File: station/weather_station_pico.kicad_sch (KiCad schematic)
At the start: 12 parts, among them J1 I2C1_EXP, J2 I2C0_EXP, U1 Pico

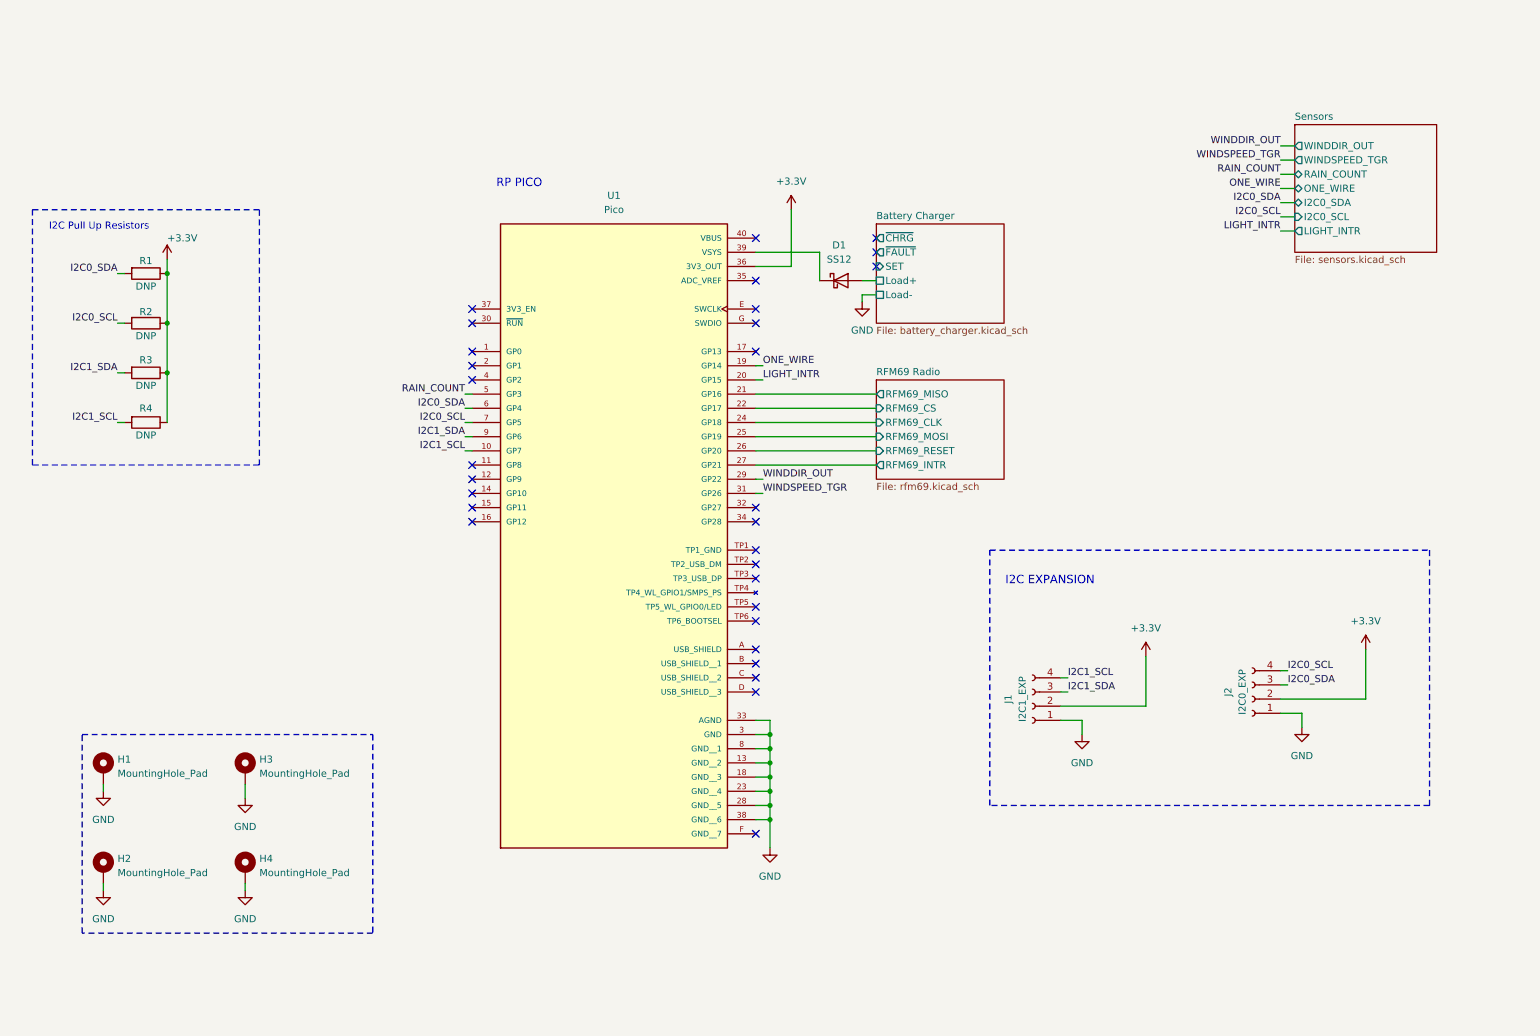
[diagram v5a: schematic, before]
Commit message: Added a reset button, status LEDs and broke out UART pins
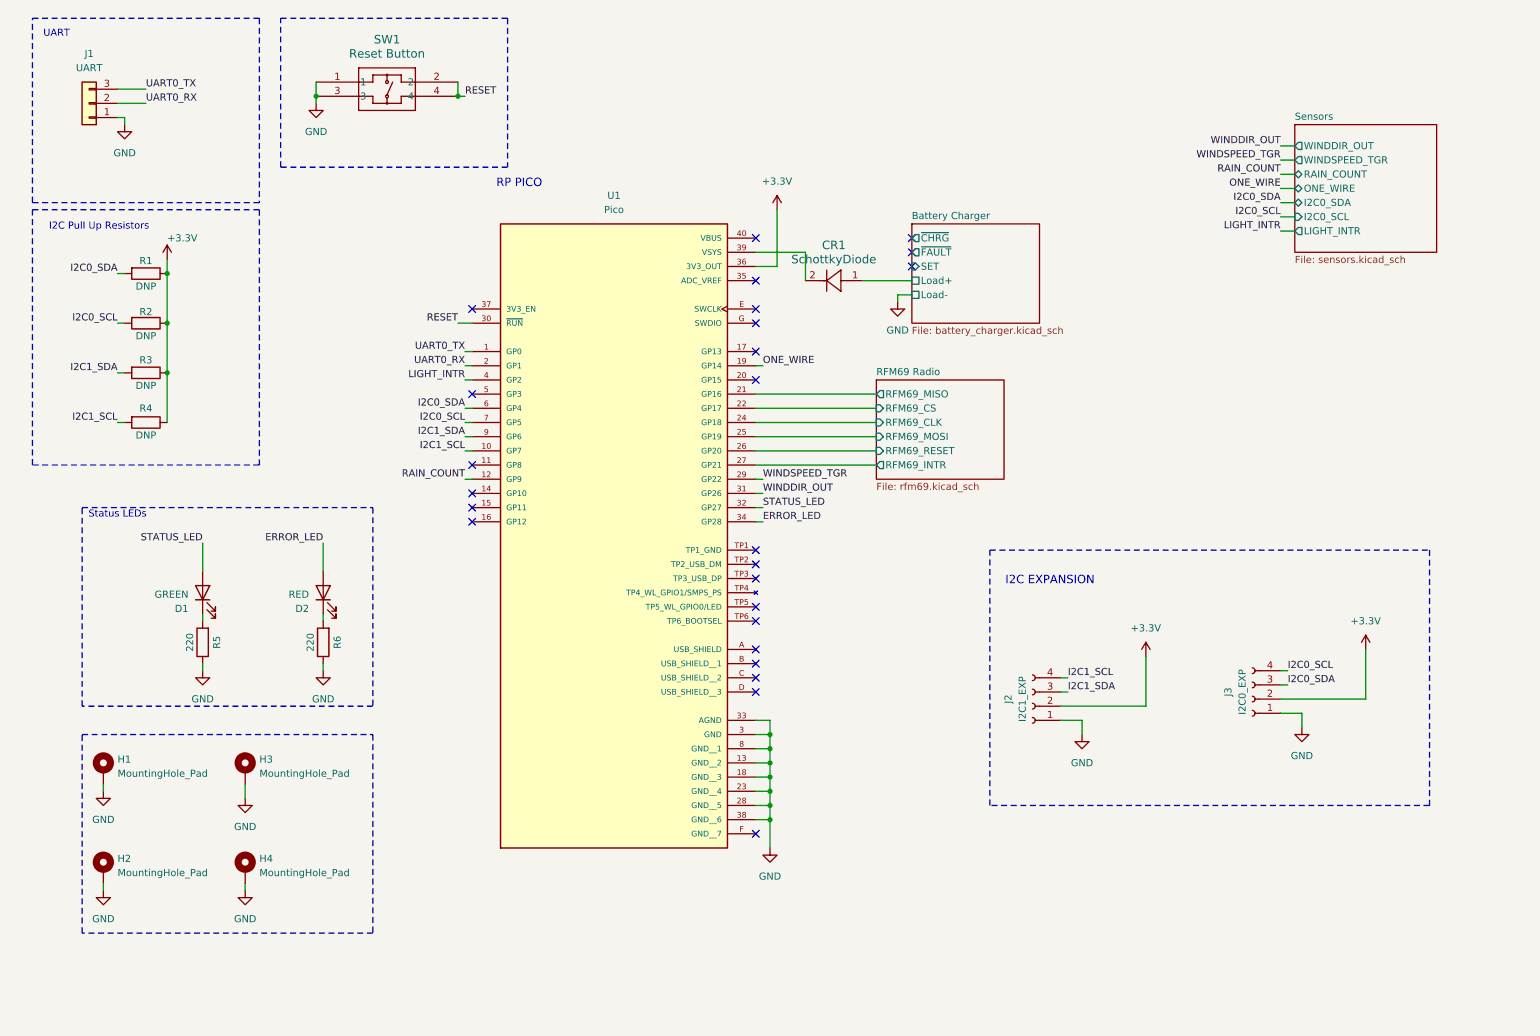
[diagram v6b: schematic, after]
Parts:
- removed D1: SS12, Diode_SMD:D_SMA, symbol Diode:SS12
- added CR1: SchottkyDiode, WeatherStation:SchottkyDiode, symbol Weather_Sensors:SchottkyDiode
- added D1: GREEN, LED_SMD:LED_0805_2012Metric_Pad1.15x1.40mm_HandSolder, symbol Device:LED
- added D2: RED, LED_SMD:LED_0805_2012Metric_Pad1.15x1.40mm_HandSolder, symbol Device:LED
- added J1: UART, Connector_PinSocket_2.54mm:PinSocket_1x03_P2.54mm_Vertical, symbol Connector_Generic:Conn_01x03
- added R5, R6: 220, Resistor_SMD:R_0805_2012Metric_Pad1.20x1.40mm_HandSolder, symbol Device:R
- added SW1: Reset Button, WeatherStation:TactileButton, symbol Weather_Sensors:TactileButton
- renumbered J1 to J2, J2 to J3
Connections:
- net Battery Charger/Load+: now also CR1.1
- net GND: now also J1.1 (Pin_1), R5.1, R6.1, SW1.1, SW1.3
- net LIGHT_INTR: now also U1.4 (GP2); no longer U1.20 (GP15)
- net RAIN_COUNT: now also U1.12 (GP9); no longer U1.5 (GP3)
- net WINDDIR_OUT: now also U1.31 (GP26); no longer U1.29 (GP22)
- net WINDSPEED_TGR: now also U1.29 (GP22); no longer U1.31 (GP26)
- net at U1.39 (VSYS): now also CR1.2
- net UART0_TX: now reaches U1.1 (GP0)
- net UART0_TX: now also J1.3 (Pin_3)
- net UART0_RX: now reaches U1.2 (GP1)
- net UART0_RX: now also J1.2 (Pin_2)
- net RESET: now reaches U1.30 (~{RUN})
- net RESET: now also SW1.2, SW1.4
- net STATUS_LED: now reaches U1.32 (GP27)
- net STATUS_LED: now also D1.2 (A)
- net ERROR_LED: now reaches U1.34 (GP28)
- net ERROR_LED: now also D2.2 (A)
- new net: D1.1 (K), R5.2
- new net: D2.1 (K), R6.2
- no-connect marks 30 -> 25
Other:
- note added: "Status LEDs"
- note added: "UART"

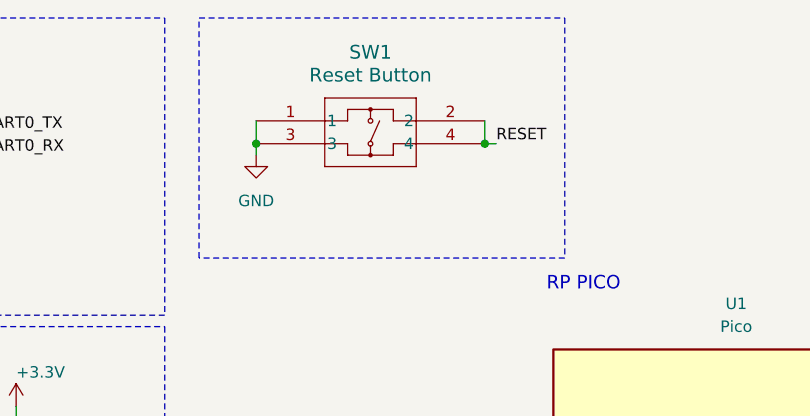
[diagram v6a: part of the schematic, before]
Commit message: Fixed a defect where to wrong pins of the reset button were shorted together, causing the pico board to be in a constant reset state
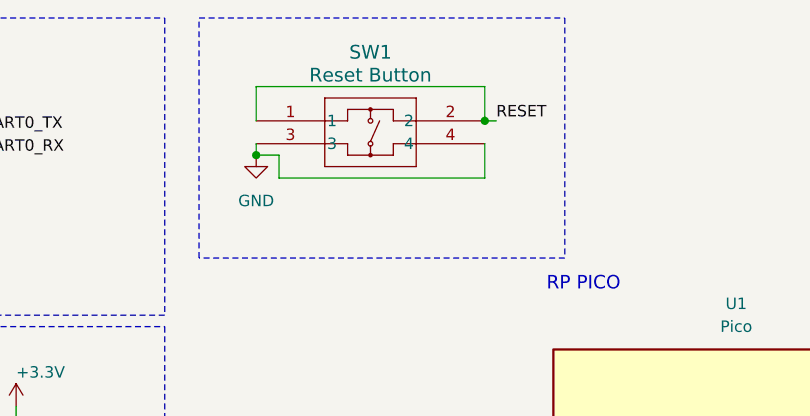
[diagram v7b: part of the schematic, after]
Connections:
- net GND: now also SW1.4; no longer SW1.1
- net RESET: now also SW1.1; no longer SW1.4
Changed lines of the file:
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@@
+	)
+	(junction
+		(at 67.31 29.21)
+		(diameter 0)
+		(color 0 0 0 0)
+	)
+	(junction
+		(at 92.71 25.4)
+		(diameter 0)
+		(color 0 0 0 0)
 	)
 	(junction
@@
 	)
 	(junction
-		(at 67.31 27.94)
-		(diameter 0)
-		(color 0 0 0 0)
-	)
-	(junction
 		(at 148.59 157.48)
-		(diameter 0)
-		(color 0 0 0 0)
-	)
-	(junction
-		(at 92.71 27.94)
 		(diameter 0)
 		(color 0 0 0 0)
@@
 	(wire
 		(pts
+			(xy 69.85 29.21) (xy 67.31 29.21)
+		)
+		(stroke
+			(width 0)
+			(type default)
+		)
+	)
+	(wire
+		(pts
 			(xy 68.58 113.03) (xy 68.58 107.95)
 		)
@@
 	(wire
 		(pts
-			(xy 92.71 25.4) (xy 92.71 27.94)
-		)
-		(stroke
-			(width 0)
-			(type default)
-		)
-	)
-	(wire
-		(pts
 			(xy 146.05 142.24) (xy 148.59 142.24)
 		)
@@
 	(wire
 		(pts
-			(xy 67.31 25.4) (xy 67.31 27.94)
-		)
-		(stroke
-			(width 0)
-			(type default)
-		)
-	)
-	(wire
-		(pts
 			(xy 93.98 88.9) (xy 95.25 88.9)
 		)
@@
 	(wire
 		(pts
-			(xy 92.71 27.94) (xy 93.98 27.94)
-		)
-		(stroke
-			(width 0)
-			(type default)
-		)
-	)
-	(wire
-		(pts
 			(xy 93.98 78.74) (xy 95.25 78.74)
 		)
@@
 	(wire
 		(pts
+			(xy 92.71 27.94) (xy 92.71 31.75)
+		)
+		(stroke
+			(width 0)
+			(type default)
+		)
+	)
+	(wire
+		(pts
 			(xy 31.75 86.36) (xy 33.02 86.36)
 		)
@@
 	(wire
 		(pts
+			(xy 67.31 21.59) (xy 92.71 21.59)
+		)
+		(stroke
+			(width 0)
+			(type default)
+		)
+	)
+	(wire
+		(pts
+			(xy 92.71 25.4) (xy 93.98 25.4)
+		)
+		(stroke
+			(width 0)
+			(type default)
+		)
+	)
+	(wire
+		(pts
 			(xy 240.03 135.89) (xy 255.27 135.89)
 		)
@@
 	(wire
 		(pts
+			(xy 67.31 25.4) (xy 67.31 21.59)
+		)
+		(stroke
+			(width 0)
+			(type default)
+		)
+	)
+	(wire
+		(pts
 			(xy 146.05 101.6) (xy 147.32 101.6)
 		)
@@
 	(wire
 		(pts
+			(xy 92.71 21.59) (xy 92.71 25.4)
+		)
+		(stroke
+			(width 0)
+			(type default)
+		)
+	)
+	(wire
+		(pts
+			(xy 69.85 31.75) (xy 69.85 29.21)
+		)
+		(stroke
+			(width 0)
+			(type default)
+		)
+	)
+	(wire
+		(pts
+			(xy 146.05 157.48) (xy 148.59 157.48)
+		)
+		(stroke
+			(width 0)
+			(type default)
+		)
+	)
+	(wire
+		(pts
+			(xy 92.71 31.75) (xy 69.85 31.75)
+		)
+		(stroke
+			(width 0)
+			(type default)
+		)
+	)
+	(wire
+		(pts
+			(xy 240.03 46.99) (xy 242.57 46.99)
+		)
+		(stroke
+			(width 0)
+			(type default)
+		)
+	)
+	(wire
+		(pts
+			(xy 46.99 120.65) (xy 46.99 121.92)
+		)
+		(stroke
+			(width 0)
+			(type default)
+		)
+	)
+	(wire
+		(pts
+			(xy 240.03 41.91) (xy 242.57 41.91)
+		)
+		(stroke
+			(width 0)
+			(type default)
+		)
+	)
+	(wire
+		(pts
 			(xy 67.31 27.94) (xy 67.31 29.21)
-		)
-		(stroke
-			(width 0)
-			(type default)
-		)
-	)
-	(wire
-		(pts
-			(xy 146.05 157.48) (xy 148.59 157.48)
-		)
-		(stroke
-			(width 0)
-			(type default)
-		)
-	)
-	(wire
-		(pts
-			(xy 240.03 46.99) (xy 242.57 46.99)
-		)
-		(stroke
-			(width 0)
-			(type default)
-		)
-	)
-	(wire
-		(pts
-			(xy 46.99 120.65) (xy 46.99 121.92)
-		)
-		(stroke
-			(width 0)
-			(type default)
-		)
-	)
-	(wire
-		(pts
-			(xy 240.03 41.91) (xy 242.57 41.91)
 		)
 		(stroke
@@
 	)
 	(label "RESET"
-		(at 93.98 27.94 0)
+		(at 93.98 25.4 0)
 		(fields_autoplaced yes)
 		(effects
